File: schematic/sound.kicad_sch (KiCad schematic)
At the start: 1 part, among them U20 SN76489AN

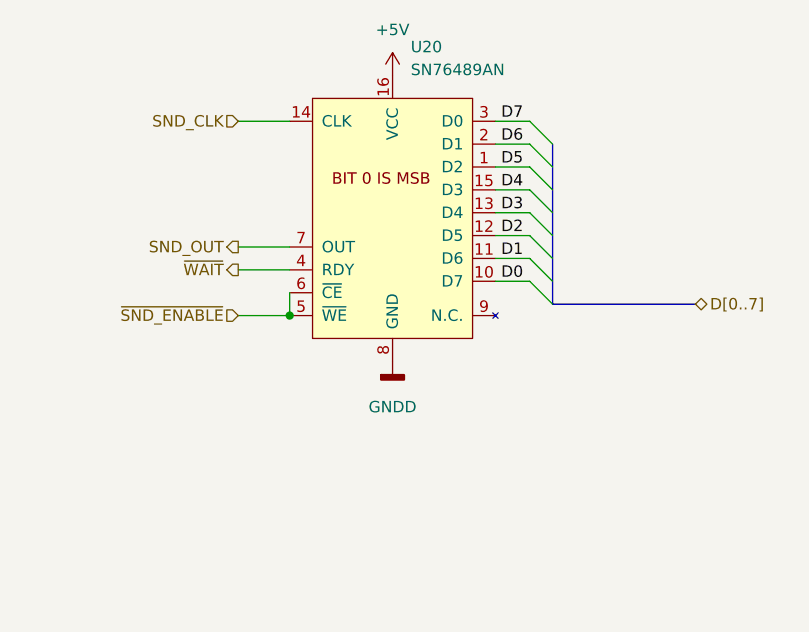
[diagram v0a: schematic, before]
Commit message: adjusted size of the sheets. added pcb version to the rev field. F.0... the 0 is for future fixes on my end. RF PCB is E.0.
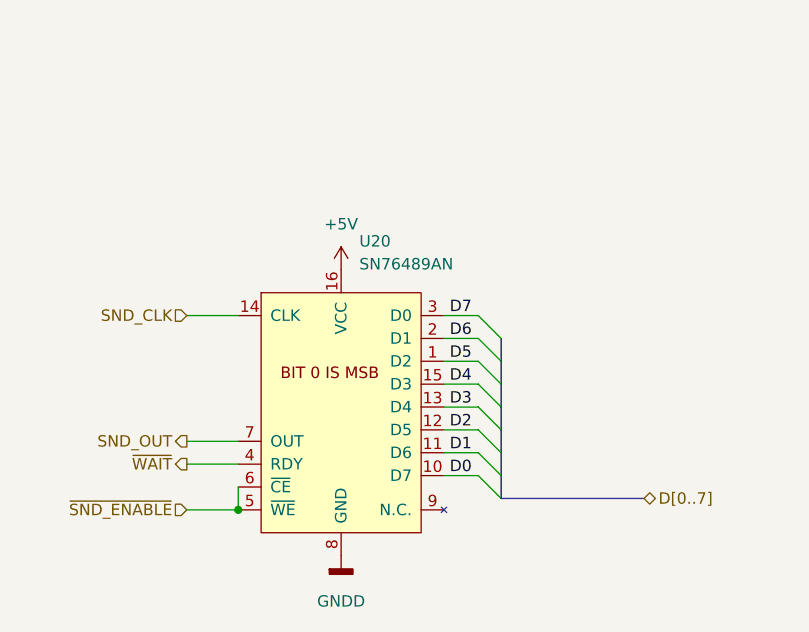
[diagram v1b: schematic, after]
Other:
- title: (none) -> Colecovision Schematic
- moved on the sheet: U20
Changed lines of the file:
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@@
 (kicad_sch (version 20211123) (generator eeschema)
-  (paper "A4")
-  (junction (at 138.43 90.17) (diameter 0) (color 0 0 0 0)
+  (paper "USLetter")
+  (title_block
+    (title "Colecovision Schematic")
+    (date "2023-01-09")
+    (rev "F.0")
+    (comment 1 "Jay Convertino")
   )
-  (bus_entry (at 165.1 78.74) (size 2.54 2.54)
+  (junction (at 132.715 111.76) (diameter 0) (color 0 0 0 0)
+  )
+  (bus_entry (at 159.385 100.33) (size 2.54 2.54)
     (stroke (width 0) (type default) (color 0 0 0 0))
   )
-  (bus_entry (at 165.1 83.82) (size 2.54 2.54)
+  (bus_entry (at 159.385 105.41) (size 2.54 2.54)
     (stroke (width 0) (type default) (color 0 0 0 0))
   )
-  (bus_entry (at 165.1 81.28) (size 2.54 2.54)
+  (bus_entry (at 159.385 102.87) (size 2.54 2.54)
     (stroke (width 0) (type default) (color 0 0 0 0))
   )
-  (bus_entry (at 165.1 71.12) (size 2.54 2.54)
+  (bus_entry (at 159.385 92.71) (size 2.54 2.54)
     (stroke (width 0) (type default) (color 0 0 0 0))
   )
-  (bus_entry (at 165.1 68.58) (size 2.54 2.54)
+  (bus_entry (at 159.385 90.17) (size 2.54 2.54)
     (stroke (width 0) (type default) (color 0 0 0 0))
   )
-  (bus_entry (at 165.1 73.66) (size 2.54 2.54)
+  (bus_entry (at 159.385 95.25) (size 2.54 2.54)
     (stroke (width 0) (type default) (color 0 0 0 0))
   )
-  (bus_entry (at 165.1 76.2) (size 2.54 2.54)
+  (bus_entry (at 159.385 97.79) (size 2.54 2.54)
     (stroke (width 0) (type default) (color 0 0 0 0))
   )
-  (bus_entry (at 165.1 86.36) (size 2.54 2.54)
+  (bus_entry (at 159.385 107.95) (size 2.54 2.54)
     (stroke (width 0) (type default) (color 0 0 0 0))
   )
-  (wire (pts (xy 161.29 86.36) (xy 165.1 86.36))
+  (wire (pts (xy 155.575 107.95) (xy 159.385 107.95))
     (stroke (width 0) (type default) (color 0 0 0 0))
   )
-  (wire (pts (xy 132.715 68.58) (xy 138.43 68.58))
+  (wire (pts (xy 127 90.17) (xy 132.715 90.17))
     (stroke (width 0) (type default) (color 0 0 0 0))
   )
-  (bus (pts (xy 167.64 81.28) (xy 167.64 83.82))
+  (bus (pts (xy 161.925 102.87) (xy 161.925 105.41))
     (stroke (width 0) (type default) (color 0 0 0 0))
   )
-  (bus (pts (xy 167.64 83.82) (xy 167.64 86.36))
+  (bus (pts (xy 161.925 105.41) (xy 161.925 107.95))
     (stroke (width 0) (type default) (color 0 0 0 0))
   )
-  (wire (pts (xy 161.29 78.74) (xy 165.1 78.74))
+  (wire (pts (xy 155.575 100.33) (xy 159.385 100.33))
     (stroke (width 0) (type default) (color 0 0 0 0))
   )
-  (wire (pts (xy 138.43 87.63) (xy 138.43 90.17))
+  (wire (pts (xy 132.715 109.22) (xy 132.715 111.76))
     (stroke (width 0) (type default) (color 0 0 0 0))
   )
-  (bus (pts (xy 167.64 88.9) (xy 183.515 88.9))
+  (bus (pts (xy 161.925 110.49) (xy 177.8 110.49))
     (stroke (width 0) (type default) (color 0 0 0 0))
   )
-  (bus (pts (xy 167.64 76.2) (xy 167.64 78.74))
+  (bus (pts (xy 161.925 97.79) (xy 161.925 100.33))
     (stroke (width 0) (type default) (color 0 0 0 0))
   )
-  (wire (pts (xy 161.29 73.66) (xy 165.1 73.66))
+  (wire (pts (xy 155.575 95.25) (xy 159.385 95.25))
     (stroke (width 0) (type default) (color 0 0 0 0))
   )
-  (bus (pts (xy 167.64 73.66) (xy 167.64 76.2))
+  (bus (pts (xy 161.925 95.25) (xy 161.925 97.79))
     (stroke (width 0) (type default) (color 0 0 0 0))
   )
-  (wire (pts (xy 132.715 85.09) (xy 138.43 85.09))
+  (wire (pts (xy 127 106.68) (xy 132.715 106.68))
     (stroke (width 0) (type default) (color 0 0 0 0))
   )
-  (bus (pts (xy 167.64 78.74) (xy 167.64 81.28))
+  (bus (pts (xy 161.925 100.33) (xy 161.925 102.87))
     (stroke (width 0) (type default) (color 0 0 0 0))
   )
-  (wire (pts (xy 161.29 71.12) (xy 165.1 71.12))
+  (wire (pts (xy 155.575 92.71) (xy 159.385 92.71))
     (stroke (width 0) (type default) (color 0 0 0 0))
   )
-  (wire (pts (xy 132.715 90.17) (xy 138.43 90.17))
+  (wire (pts (xy 127 111.76) (xy 132.715 111.76))
     (stroke (width 0) (type default) (color 0 0 0 0))
   )
-  (bus (pts (xy 167.64 86.36) (xy 167.64 88.9))
+  (bus (pts (xy 161.925 107.95) (xy 161.925 110.49))
     (stroke (width 0) (type default) (color 0 0 0 0))
   )
-  (bus (pts (xy 167.64 71.12) (xy 167.64 73.66))
+  (bus (pts (xy 161.925 92.71) (xy 161.925 95.25))
     (stroke (width 0) (type default) (color 0 0 0 0))
   )
-  (wire (pts (xy 161.29 76.2) (xy 165.1 76.2))
+  (wire (pts (xy 155.575 97.79) (xy 159.385 97.79))
     (stroke (width 0) (type default) (color 0 0 0 0))
   )
-  (wire (pts (xy 161.29 81.28) (xy 165.1 81.28))
+  (wire (pts (xy 155.575 102.87) (xy 159.385 102.87))
     (stroke (width 0) (type default) (color 0 0 0 0))
   )
-  (wire (pts (xy 161.29 68.58) (xy 165.1 68.58))
+  (wire (pts (xy 155.575 90.17) (xy 159.385 90.17))
     (stroke (width 0) (type default) (color 0 0 0 0))
   )
-  (wire (pts (xy 132.715 82.55) (xy 138.43 82.55))
+  (wire (pts (xy 127 104.14) (xy 132.715 104.14))
     (stroke (width 0) (type default) (color 0 0 0 0))
   )
-  (wire (pts (xy 161.29 83.82) (xy 165.1 83.82))
+  (wire (pts (xy 155.575 105.41) (xy 159.385 105.41))
     (stroke (width 0) (type default) (color 0 0 0 0))
   )
-  (label "D3" (at 161.925 78.74 0)
+  (label "D3" (at 156.21 100.33 0)
     (effects (font (size 1.27 1.27)) (justify left bottom))
   )
-  (label "D0" (at 161.925 86.36 0)
+  (label "D0" (at 156.21 107.95 0)
     (effects (font (size 1.27 1.27)) (justify left bottom))
   )
-  (label "D5" (at 161.925 73.66 0)
+  (label "D5" (at 156.21 95.25 0)
     (effects (font (size 1.27 1.27)) (justify left bottom))
   )
-  (label "D1" (at 161.925 83.82 0)
+  (label "D1" (at 156.21 105.41 0)
     (effects (font (size 1.27 1.27)) (justify left bottom))
   )
-  (label "D6" (at 161.925 71.12 0)
+  (label "D6" (at 156.21 92.71 0)
     (effects (font (size 1.27 1.27)) (justify left bottom))
   )
-  (label "D4" (at 161.925 76.2 0)
+  (label "D4" (at 156.21 97.79 0)
     (effects (font (size 1.27 1.27)) (justify left bottom))
   )
-  (label "D7" (at 161.925 68.58 0)
+  (label "D7" (at 156.21 90.17 0)
     (effects (font (size 1.27 1.27)) (justify left bottom))
   )
-  (label "D2" (at 161.925 81.28 0)
+  (label "D2" (at 156.21 102.87 0)
     (effects (font (size 1.27 1.27)) (justify left bottom))
   )
-  (hierarchical_label "D[0..7]" (shape bidirectional) (at 183.515 88.9 0)
+  (hierarchical_label "D[0..7]" (shape bidirectional) (at 177.8 110.49 0)
     (effects (font (size 1.27 1.27)) (justify left))
   )
-  (hierarchical_label "~{SND_ENABLE}" (shape input) (at 132.715 90.17 180)
+  (hierarchical_label "~{SND_ENABLE}" (shape input) (at 127 111.76 180)
     (effects (font (size 1.27 1.27)) (justify right))
   )
-  (hierarchical_label "SND_OUT" (shape output) (at 132.715 82.55 180)
+  (hierarchical_label "SND_OUT" (shape output) (at 127 104.14 180)
     (effects (font (size 1.27 1.27)) (justify right))
   )
-  (hierarchical_label "SND_CLK" (shape input) (at 132.715 68.58 180)
+  (hierarchical_label "SND_CLK" (shape input) (at 127 90.17 180)
     (effects (font (size 1.27 1.27)) (justify right))
   )
-  (hierarchical_label "~{WAIT}" (shape output) (at 132.715 85.09 180)
+  (hierarchical_label "~{WAIT}" (shape output) (at 127 106.68 180)
     (effects (font (size 1.27 1.27)) (justify right))
   )
-  (symbol (lib_id "power:GNDD") (at 149.86 95.25 0) (unit 1)
+  (symbol (lib_id "power:GNDD") (at 144.145 116.84 0) (unit 1)
     (in_bom yes) (on_board yes) (fields_autoplaced)
-    (property "Reference" "#PWR?" (id 0) (at 149.86 101.6 0)
+    (property "Reference" "#PWR?" (id 0) (at 144.145 123.19 0)
       (effects (font (size 1.27 1.27)) hide)
     )
-    (property "Value" "GNDD" (id 1) (at 149.86 100.33 0))
-    (property "Footprint" "" (id 2) (at 149.86 95.25 0)
+    (property "Value" "GNDD" (id 1) (at 144.145 121.92 0))
+    (property "Footprint" "" (id 2) (at 144.145 116.84 0)
       (effects (font (size 1.27 1.27)) hide)
     )
-    (property "Datasheet" "" (id 3) (at 149.86 95.25 0)
+    (property "Datasheet" "" (id 3) (at 144.145 116.84 0)
       (effects (font (size 1.27 1.27)) hide)
     )
     (pin "1")
   )
-  (symbol (lib_id "power:+5V") (at 149.86 63.5 0) (unit 1)
+  (symbol (lib_id "power:+5V") (at 144.145 85.09 0) (unit 1)
     (in_bom yes) (on_board yes) (fields_autoplaced)
-    (property "Reference" "#PWR?" (id 0) (at 149.86 67.31 0)
+    (property "Reference" "#PWR?" (id 0) (at 144.145 88.9 0)
       (effects (font (size 1.27 1.27)) hide)
     )
-    (property "Value" "+5V" (id 1) (at 149.86 58.42 0))
-    (property "Footprint" "" (id 2) (at 149.86 63.5 0)
+    (property "Value" "+5V" (id 1) (at 144.145 80.01 0))
+    (property "Footprint" "" (id 2) (at 144.145 85.09 0)
       (effects (font (size 1.27 1.27)) hide)
     )
-    (property "Datasheet" "" (id 3) (at 149.86 63.5 0)
+    (property "Datasheet" "" (id 3) (at 144.145 85.09 0)
       (effects (font (size 1.27 1.27)) hide)
     )
     (pin "1")
   )
-  (symbol (lib_id "Vintage_Audio_Synth:SN76489AN") (at 149.86 69.85 0) (unit 1)
+  (symbol (lib_id "Vintage_Audio_Synth:SN76489AN") (at 144.145 91.44 0) (unit 1)
     (in_bom yes) (on_board yes) (fields_autoplaced)
-    (property "Reference" "U20" (id 0) (at 151.8794 60.325 0)
+    (property "Reference" "U20" (id 0) (at 146.1644 81.915 0)
       (effects (font (size 1.27 1.27)) (justify left))
     )
-    (property "Value" "SN76489AN" (id 1) (at 151.8794 62.865 0)
+    (property "Value" "SN76489AN" (id 1) (at 146.1644 84.455 0)
       (effects (font (size 1.27 1.27)) (justify left))
     )
-    (property "Footprint" "" (id 2) (at 127 71.12 0)
+    (property "Footprint" "" (id 2) (at 121.285 92.71 0)
       (effects (font (size 1.27 1.27)) hide)
     )
-    (property "Datasheet" "" (id 3) (at 127 71.12 0)
+    (property "Datasheet" "" (id 3) (at 121.285 92.71 0)
       (effects (font (size 1.27 1.27)) hide)
     )

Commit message: cleanup, and started associating components
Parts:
- U20: footprint (none) -> Package_DIP:DIP-16_W7.62mm_LongPads
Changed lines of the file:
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@@
   (symbol (lib_id "power:GNDD") (at 144.145 116.84 0) (unit 1)
     (in_bom yes) (on_board yes) (fields_autoplaced)
-    (property "Reference" "#PWR?" (id 0) (at 144.145 123.19 0)
+    (property "Reference" "#PWR0124" (id 0) (at 144.145 123.19 0)
       (effects (font (size 1.27 1.27)) hide)
     )
@@
   (symbol (lib_id "power:+5V") (at 144.145 85.09 0) (unit 1)
     (in_bom yes) (on_board yes) (fields_autoplaced)
-    (property "Reference" "#PWR?" (id 0) (at 144.145 88.9 0)
+    (property "Reference" "#PWR0125" (id 0) (at 144.145 88.9 0)
       (effects (font (size 1.27 1.27)) hide)
     )
@@
       (effects (font (size 1.27 1.27)) (justify left))
     )
-    (property "Footprint" "" (id 2) (at 121.285 92.71 0)
+    (property "Footprint" "Package_DIP:DIP-16_W7.62mm_LongPads" (id 2) (at 121.285 92.71 0)
       (effects (font (size 1.27 1.27)) hide)
     )

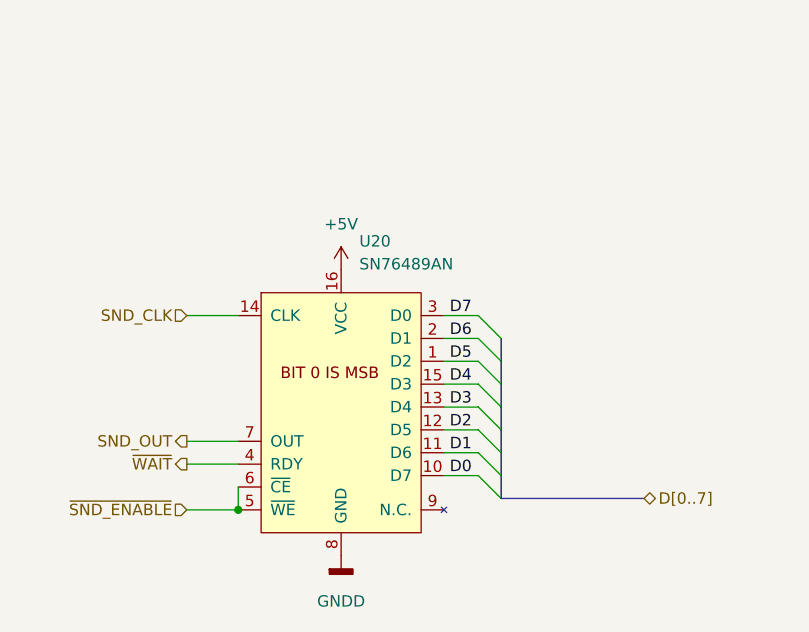
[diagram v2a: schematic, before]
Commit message: first draft of board with components added, no traces
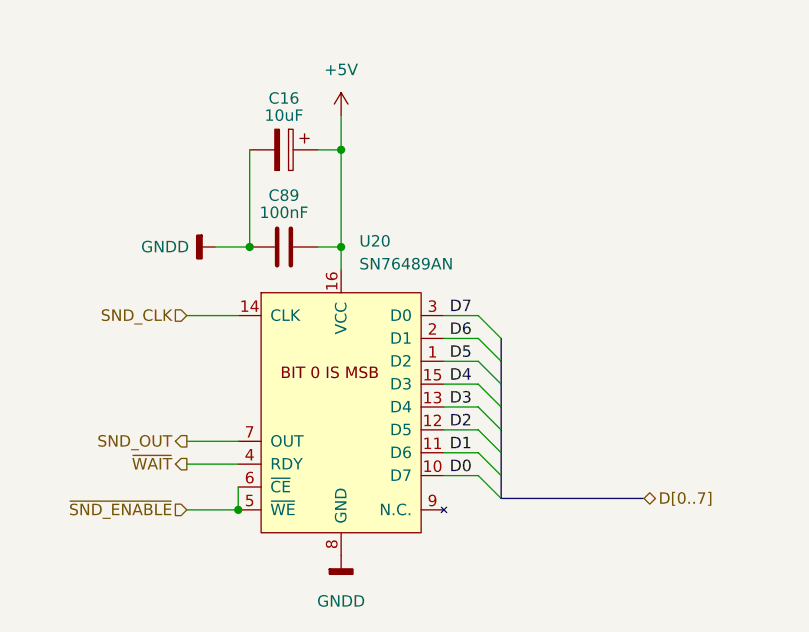
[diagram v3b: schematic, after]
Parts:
- added C16: 10uF, Capacitor_THT:CP_Radial_D5.0mm_P2.50mm, symbol Device:C_Polarized
- added C89: 100nF, Capacitor_THT:C_Disc_D7.0mm_W2.5mm_P5.00mm, symbol Device:C
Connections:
- net +5V: now also C16.1, C89.1
- net GNDD: now also C16.2, C89.2
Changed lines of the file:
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@@
     (comment 1 "Jay Convertino")
   )
+  (junction (at 133.985 82.55) (diameter 0) (color 0 0 0 0)
+  )
+  (junction (at 144.145 71.755) (diameter 0) (color 0 0 0 0)
+  )
   (junction (at 132.715 111.76) (diameter 0) (color 0 0 0 0)
   )
+  (junction (at 144.145 82.55) (diameter 0) (color 0 0 0 0)
+  )
   (bus_entry (at 159.385 100.33) (size 2.54 2.54)
     (stroke (width 0) (type default) (color 0 0 0 0))
@@
     (stroke (width 0) (type default) (color 0 0 0 0))
   )
+  (wire (pts (xy 141.605 82.55) (xy 144.145 82.55))
+    (stroke (width 0) (type default) (color 0 0 0 0))
+  )
   (bus (pts (xy 161.925 105.41) (xy 161.925 107.95))
     (stroke (width 0) (type default) (color 0 0 0 0))
@@
     (stroke (width 0) (type default) (color 0 0 0 0))
   )
+  (wire (pts (xy 141.605 71.755) (xy 144.145 71.755))
+    (stroke (width 0) (type default) (color 0 0 0 0))
+  )
   (bus (pts (xy 161.925 100.33) (xy 161.925 102.87))
     (stroke (width 0) (type default) (color 0 0 0 0))
@@
     (stroke (width 0) (type default) (color 0 0 0 0))
   )
+  (wire (pts (xy 144.145 71.755) (xy 144.145 82.55))
+    (stroke (width 0) (type default) (color 0 0 0 0))
+  )
+  (wire (pts (xy 133.985 71.755) (xy 133.985 82.55))
+    (stroke (width 0) (type default) (color 0 0 0 0))
+  )
+  (wire (pts (xy 144.145 82.55) (xy 144.145 85.09))
+    (stroke (width 0) (type default) (color 0 0 0 0))
+  )
+  (wire (pts (xy 130.175 82.55) (xy 133.985 82.55))
+    (stroke (width 0) (type default) (color 0 0 0 0))
+  )
   (wire (pts (xy 155.575 97.79) (xy 159.385 97.79))
     (stroke (width 0) (type default) (color 0 0 0 0))
   )
   (wire (pts (xy 155.575 102.87) (xy 159.385 102.87))
+    (stroke (width 0) (type default) (color 0 0 0 0))
+  )
+  (wire (pts (xy 144.145 67.945) (xy 144.145 71.755))
     (stroke (width 0) (type default) (color 0 0 0 0))
   )
@@
   (hierarchical_label "~{WAIT}" (shape output) (at 127 106.68 180)
     (effects (font (size 1.27 1.27)) (justify right))
+  )
+  (symbol (lib_id "Device:C") (at 137.795 82.55 270) (unit 1)
+    (in_bom yes) (on_board yes)
+    (property "Reference" "C89" (id 0) (at 137.795 76.835 90))
+    (property "Value" "100nF" (id 1) (at 137.795 78.74 90))
+    (property "Footprint" "Capacitor_THT:C_Disc_D7.0mm_W2.5mm_P5.00mm" (id 2) (at 133.985 83.5152 0)
+      (effects (font (size 1.27 1.27)) hide)
+    )
+    (property "Datasheet" "~" (id 3) (at 137.795 82.55 0)
+      (effects (font (size 1.27 1.27)) hide)
+    )
+    (pin "1")
+    (pin "2")
   )
   (symbol (lib_id "power:GNDD") (at 144.145 116.84 0) (unit 1)
@@
     (pin "1")
   )
-  (symbol (lib_id "power:+5V") (at 144.145 85.09 0) (unit 1)
+  (symbol (lib_id "Device:C_Polarized") (at 137.795 71.755 270) (unit 1)
+    (in_bom yes) (on_board yes)
+    (property "Reference" "C16" (id 0) (at 137.795 66.04 90))
+    (property "Value" "10uF" (id 1) (at 137.795 67.945 90))
+    (property "Footprint" "Capacitor_THT:CP_Radial_D5.0mm_P2.50mm" (id 2) (at 133.985 72.7202 0)
+      (effects (font (size 1.27 1.27)) hide)
+    )
+    (property "Datasheet" "~" (id 3) (at 137.795 71.755 0)
+      (effects (font (size 1.27 1.27)) hide)
+    )
+    (pin "1")
+    (pin "2")
+  )
+  (symbol (lib_id "power:+5V") (at 144.145 67.945 0) (unit 1)
     (in_bom yes) (on_board yes) (fields_autoplaced)
-    (property "Reference" "#PWR0125" (id 0) (at 144.145 88.9 0)
-      (effects (font (size 1.27 1.27)) hide)
-    )
-    (property "Value" "+5V" (id 1) (at 144.145 80.01 0))
-    (property "Footprint" "" (id 2) (at 144.145 85.09 0)
-      (effects (font (size 1.27 1.27)) hide)
-    )
-    (property "Datasheet" "" (id 3) (at 144.145 85.09 0)
+    (property "Reference" "#PWR0125" (id 0) (at 144.145 71.755 0)
+      (effects (font (size 1.27 1.27)) hide)
+    )
+    (property "Value" "+5V" (id 1) (at 144.145 62.865 0))
+    (property "Footprint" "" (id 2) (at 144.145 67.945 0)
+      (effects (font (size 1.27 1.27)) hide)
+    )
+    (property "Datasheet" "" (id 3) (at 144.145 67.945 0)
       (effects (font (size 1.27 1.27)) hide)
     )
@@
     (pin "9")
   )
+  (symbol (lib_id "power:GNDD") (at 130.175 82.55 270) (unit 1)
+    (in_bom yes) (on_board yes)
+    (property "Reference" "#PWR0265" (id 0) (at 123.825 82.55 0)
+      (effects (font (size 1.27 1.27)) hide)
+    )
+    (property "Value" "GNDD" (id 1) (at 121.92 82.55 90)
+      (effects (font (size 1.27 1.27)) (justify left))
+    )
+    (property "Footprint" "" (id 2) (at 130.175 82.55 0)
+      (effects (font (size 1.27 1.27)) hide)
+    )
+    (property "Datasheet" "" (id 3) (at 130.175 82.55 0)
+      (effects (font (size 1.27 1.27)) hide)
+    )
+    (pin "1")
+  )
 )

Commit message: added memory, eprom and sound lines. some video as well. fixed the cap size for polar. its a bit weird since they use 5 mm pin and 5mm body and bend out the leads.
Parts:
- C16: footprint Capacitor_THT:CP_Radial_D5.0mm_P2.50mm -> Capacitor_THT:CP_Radial_Tantal_D4.5mm_P5.00mm
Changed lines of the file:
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@@
     (property "Reference" "C16" (id 0) (at 137.795 66.04 90))
     (property "Value" "10uF" (id 1) (at 137.795 67.945 90))
-    (property "Footprint" "Capacitor_THT:CP_Radial_D5.0mm_P2.50mm" (id 2) (at 133.985 72.7202 0)
+    (property "Footprint" "Capacitor_THT:CP_Radial_Tantal_D4.5mm_P5.00mm" (id 2) (at 133.985 72.7202 0)
       (effects (font (size 1.27 1.27)) hide)
     )

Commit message: added new models, fixed the drc errors. changed power width.
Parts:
- C16: footprint Capacitor_THT:CP_Radial_Tantal_D4.5mm_P5.00mm -> Capacitor_THT:CP_Radial_D8.0mm_P5.00mm
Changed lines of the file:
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@@
     (property "Reference" "C16" (id 0) (at 137.795 66.04 90))
     (property "Value" "10uF" (id 1) (at 137.795 67.945 90))
-    (property "Footprint" "Capacitor_THT:CP_Radial_Tantal_D4.5mm_P5.00mm" (id 2) (at 133.985 72.7202 0)
+    (property "Footprint" "Capacitor_THT:CP_Radial_D8.0mm_P5.00mm" (id 2) (at 133.985 72.7202 0)
       (effects (font (size 1.27 1.27)) hide)
     )

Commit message: updated schematic with new layout
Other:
- company: (none) -> sparkletron
- title: Colecovision Schematic -> Reverse Engineer Colecovision
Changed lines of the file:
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@@
   (paper "USLetter")
   (title_block
-    (title "Colecovision Schematic")
-    (date "2023-01-09")
-    (rev "F.0")
+    (title "Reverse Engineer Colecovision")
+    (date "2023-03-14")
+    (rev "DEV")
+    (company "sparkletron")
     (comment 1 "Jay Convertino")
+    (comment 2 "MIT LICENSE")
   )
   (junction (at 133.985 82.55) (diameter 0) (color 0 0 0 0)
